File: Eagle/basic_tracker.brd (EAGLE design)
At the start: 73.3 x 40.6 mm, 23 parts, among them CN1 BATTERY, IC1 MCP1700 3.3v, X1 SMA

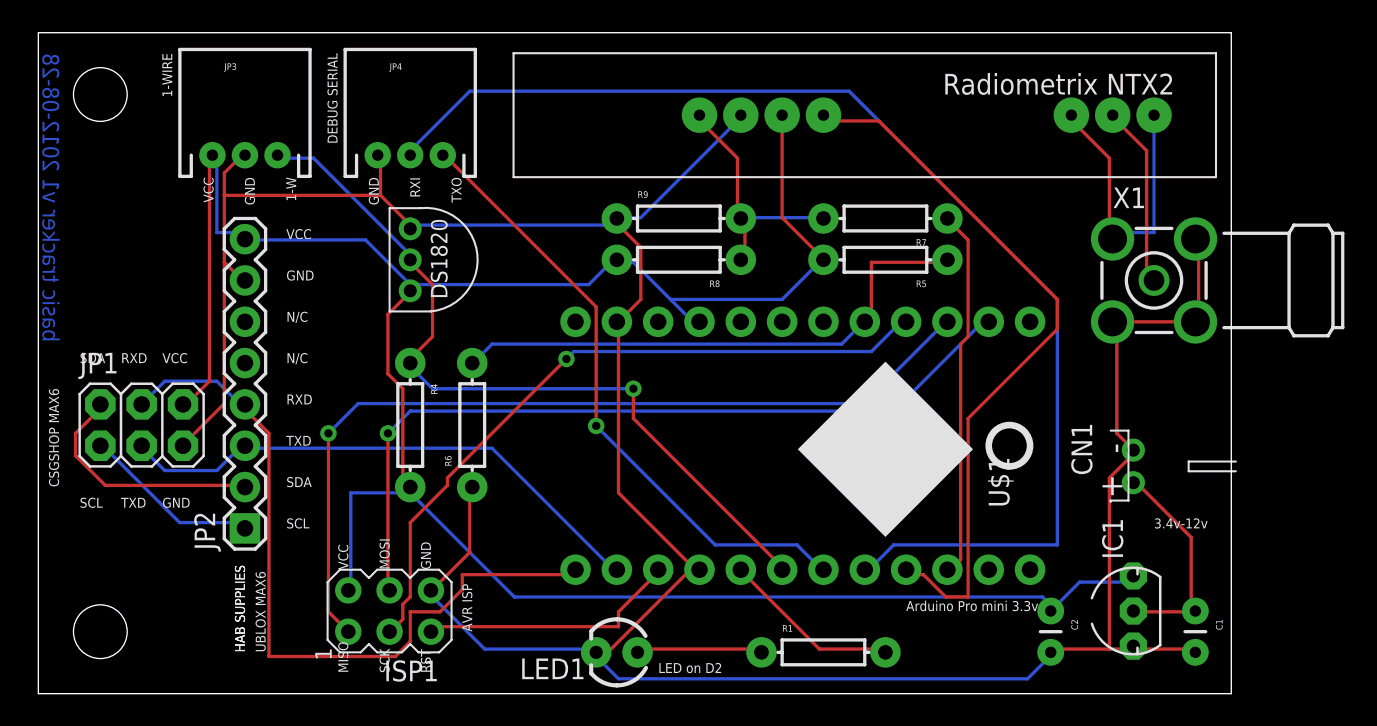
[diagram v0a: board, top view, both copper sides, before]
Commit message: Updated board text and cap sizes
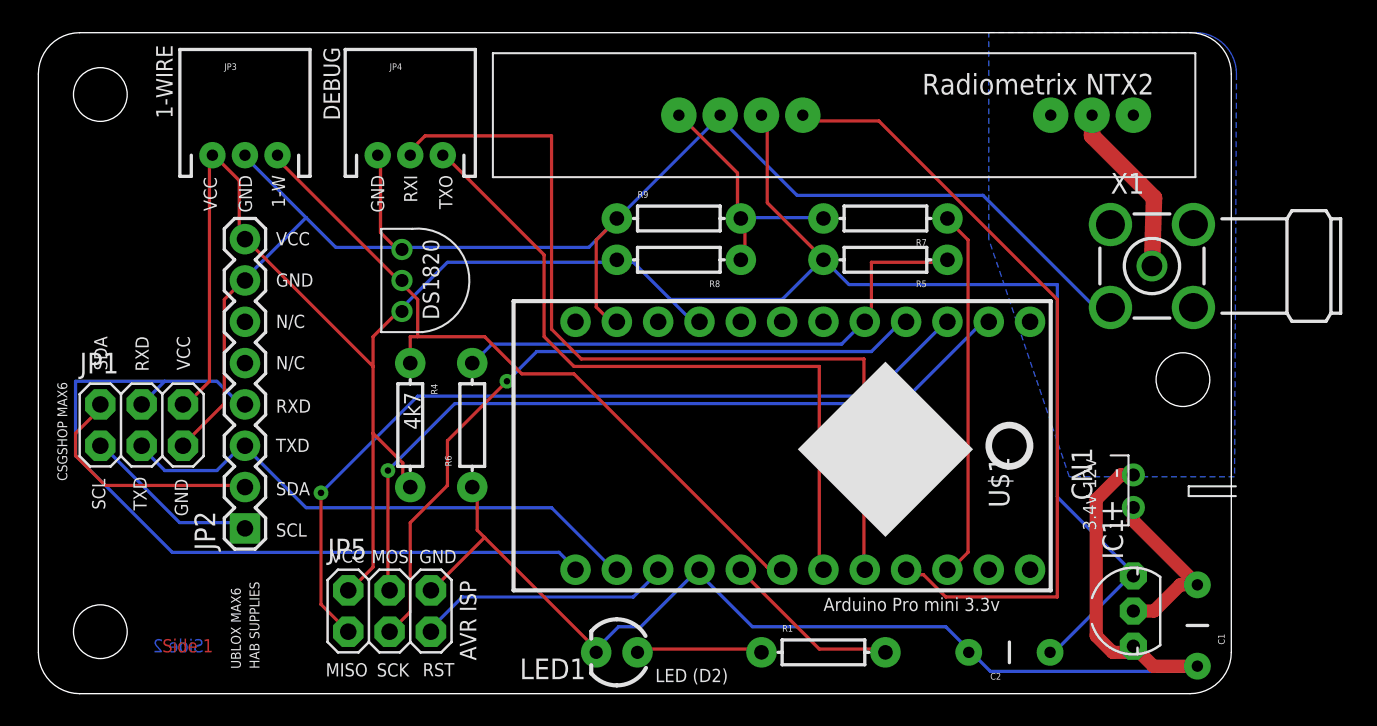
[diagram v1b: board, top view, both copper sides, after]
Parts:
- removed ISP1: AVRISP-6, adafruit:AVRISP
- added JP5: ISP, SparkFun:2X03
- added U$6: (no value), SparkFun:STAND-OFF
- C1, C2: device SparkFun:CAP-PTH-SMALL -> SparkFun:CAP-PTH-5MM
- moved C2 3.59 mm to (59.7, 2.54), turned to 180 degrees
- moved CN1 1.52 mm to (67.3, 12.4)
- moved U$2 1.37 mm to (23.6, 27.9)
- moved U$3 1.27 mm to (59.7, 35.6)
- moved X1 0.90 mm to (68.5, 26.3)
- moved C1 0.90 mm to (71.2, 4.19)
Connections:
- removed net N$5: U$3.RFGND1, U$3.RFGND2, X1.2
- net GND: now also JP5.6, U$3.RFGND1, U$3.RFGND2, X1.2; no longer ISP1.6
- net MISO: now also JP5.1; no longer ISP1.1
- net MOSI: now also JP5.4; no longer ISP1.4
- net RST: now also JP5.5; no longer ISP1.5
- net SCK: now also JP5.3; no longer ISP1.3
- net VCC: now also JP5.2; no longer ISP1.2
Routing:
- net SS_RXI: track 74.4 -> 54.2 mm
- net N$5: track 18.6 -> 0.00 mm
- net GND: track 183.1 -> 175.1 mm
- net VCC: track 147.7 -> 140.3 mm
- net SS_TXO: track 38.2 -> 44.1 mm, vias 1 -> 0
- net GPS_RXD: track 46.3 -> 51.2 mm
- net NTX_EN: track 44.3 -> 48.8 mm
- net 1-WIRE: track 47.9 -> 45.4 mm, vias 1 -> 0
- net RAW: track 13.3 -> 11.0 mm
- net MISO: track 53.6 -> 52.1 mm
- net SCK: track 43.1 -> 44.4 mm
- net MOSI: track 49.5 -> 48.1 mm
- net N$6: track 15.3 -> 15.8 mm
- net RST: track 16.2 -> 15.7 mm
- added copper zone on layer 16, net GND
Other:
- outline, holes or cut-outs redrawn
- board text added: "2012-08-29"
- board text added: "DEBUG"
- board text added: "LED (D2)"
- board text added: "Side 1"
- board text added: "Side 2"
- board text added: "basic tracker v1"
- board text removed: "DEBUG SERIAL"
- board text removed: "LED on D2"
- board text removed: "basic tracker v1 2012-08-28"

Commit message: Added a slightly modified version of the CAM file, tweaked the board and rerouted a few traces by hand
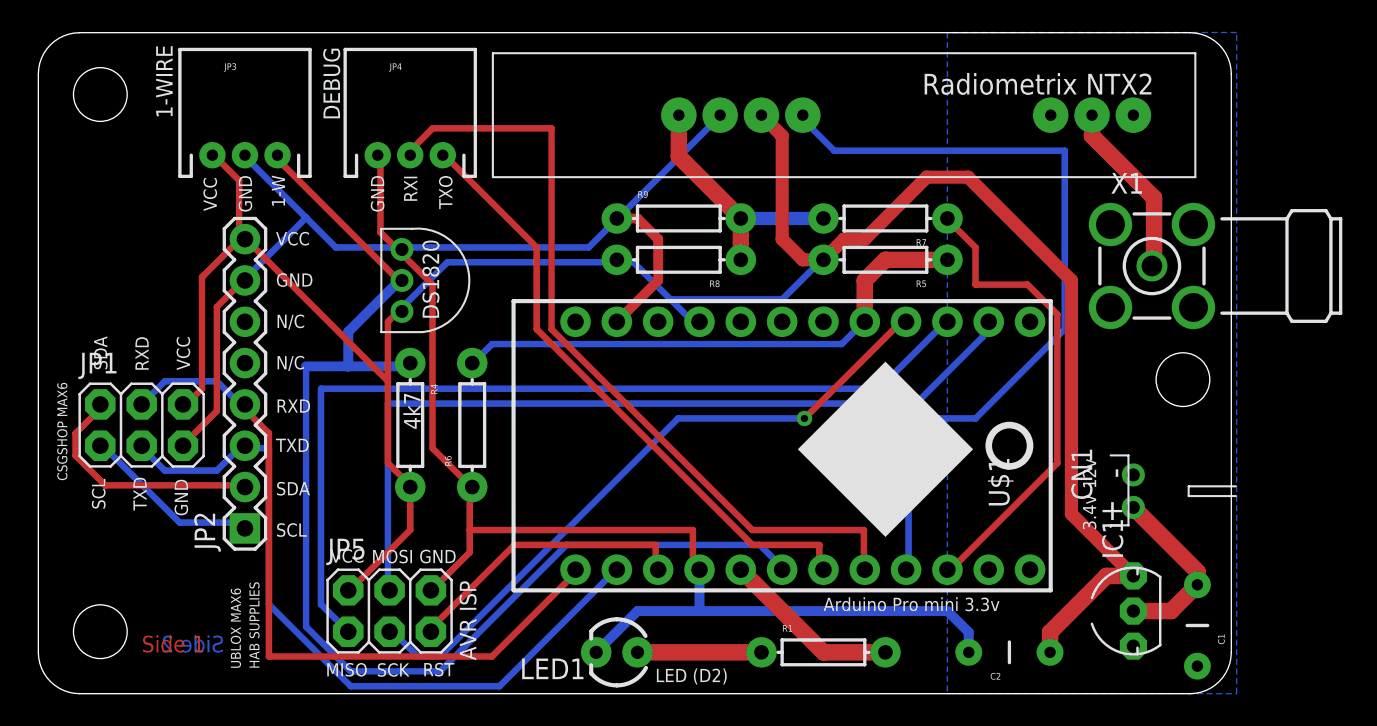
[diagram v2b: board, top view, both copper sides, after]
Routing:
- net GND: track 175.1 -> 136.5 mm
- net 1-WIRE: track 45.4 -> 74.7 mm
- net GPS_TXD: track 33.6 -> 45.2 mm
- net GPS_RXD: track 51.2 -> 44.7 mm
- net SS_TXO: track 44.1 -> 37.7 mm
- net NTX_TX: track 22.7 -> 29.1 mm
- net SS_RXI: track 54.2 -> 48.6 mm
- net MISO: track 52.1 -> 55.8 mm, vias 1 -> 0
- net SCK: track 44.4 -> 40.9 mm
- net MOSI: track 48.1 -> 51.1 mm, vias 1 -> 0
- net RST: track 15.7 -> 17.7 mm
- net BATT_ADC: track 34.0 -> 33.3 mm
- net RAW: track 11.0 -> 11.5 mm
- net NTX_EN: track 48.8 -> 49.3 mm
